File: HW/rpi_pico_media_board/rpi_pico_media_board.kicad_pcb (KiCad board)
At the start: 4 copper layers, 100 x 80 mm, 138 parts, among them J100 Barrel_Jack_Switch_Pin3Ring, J200 Conn_01x04_Pin, J201 Conn_01x04_Pin, J300 AudioJack3_Ground_SwitchTR, J301 Conn_01x03_Pin, J400 TF-01A, Q100 T2N7002AK, Q500 T2N7002AK, Q501 T2N7002AK, Q502 T2N7002AK, SW200 SW_DPDT_XLX, U100 HT7533-1, U101 HT7533-1, U200 RaspberryPi_Pico, U202 mems-mic, U203 mems-mic, U300 PCM5102A, U500 SW, U501 SW, U502 SW, U503 SW, U504 SW, U505 SW, U506 SW, U507 SW, U508 SW, U509 SW, U510 SW, U511 SW, U600 PCF8563TS, Y600 32768Hz

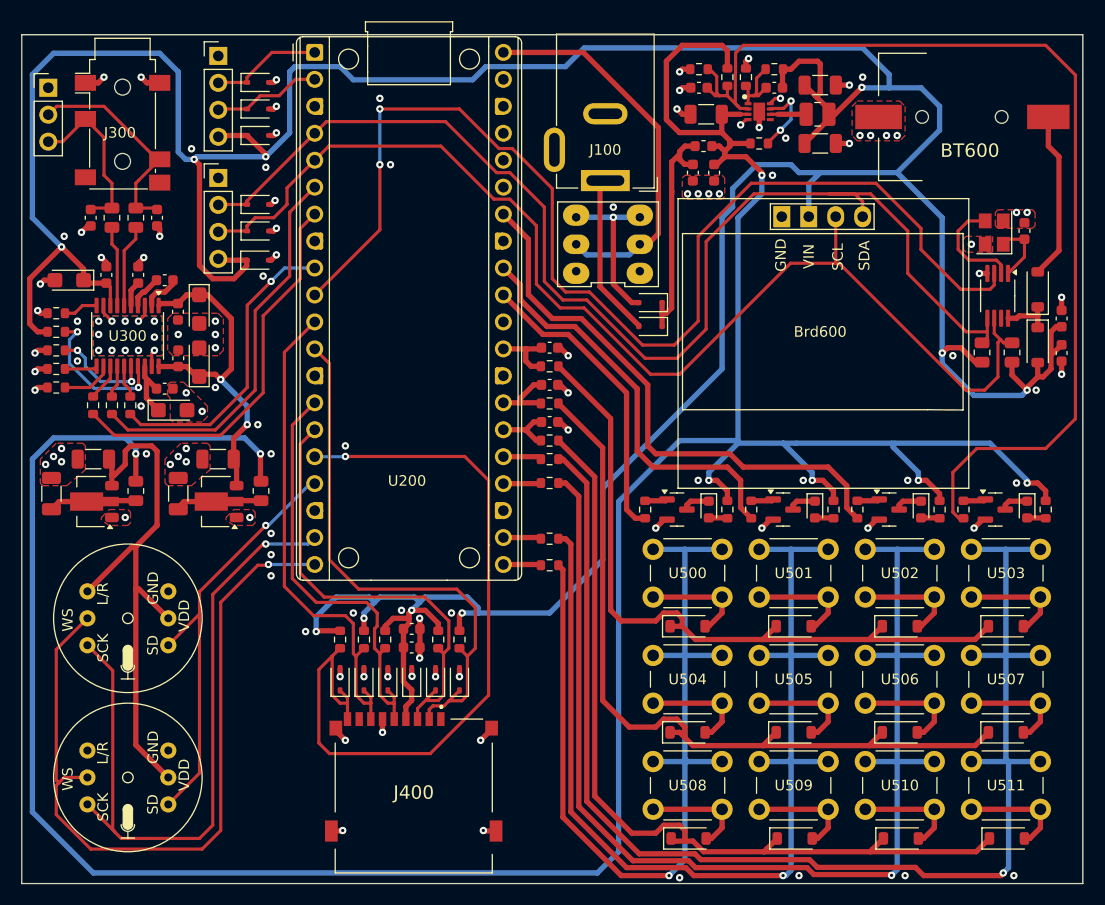
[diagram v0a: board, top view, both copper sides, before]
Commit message: Minor PCB layout updates
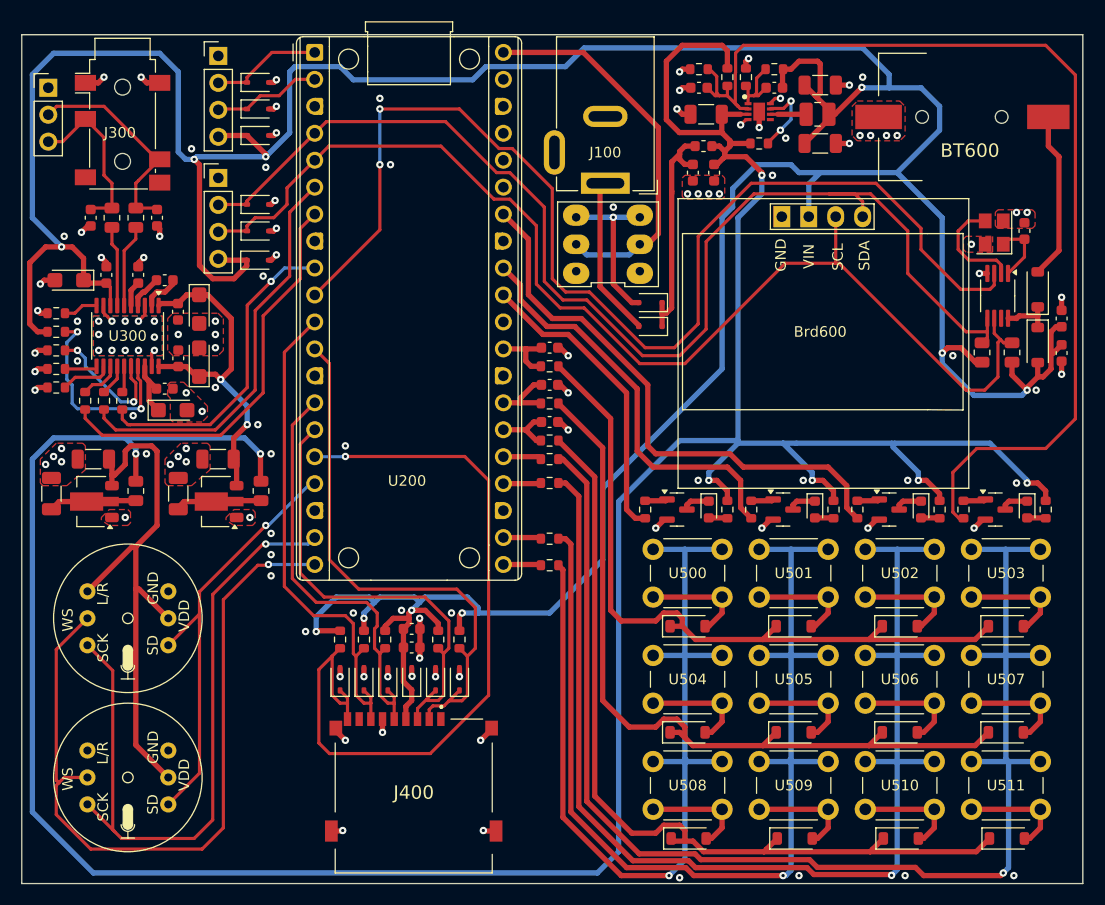
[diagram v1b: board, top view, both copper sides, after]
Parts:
- moved R300 0.86 mm to (59.5, 84.5)
- moved R301 0.86 mm to (57.8, 84.5)
- moved R302 0.86 mm to (56.0, 84.5)
- moved J100 0.25 mm to (105.0, 64.0)
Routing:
- net /[3]PCM5102/XSMT: track 14.7 -> 20.0 mm
- net /[3]PCM5102/FMT: track 10.4 -> 13.6 mm
- net I2S_PCM5102_SCL: track 28.5 -> 30.1 mm
- net +3.3V: track 368.0 -> 369.5 mm
- net I2S_PCM5102_DATA: track 37.1 -> 38.5 mm
- net I2S_PCM5102_SCK: track 37.4 -> 38.8 mm
- net I2C1_SCL: track 111.4 -> 110.6 mm
- net /[3]PCM5102/LRCLK: track 3.09 -> 2.50 mm

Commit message: Trace length tuning
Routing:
- net I2S_INMP441_DATA: track 41.4 -> 69.2 mm
- net SPI1_SD_CARD_SCK: track 40.2 -> 52.9 mm
- net SPI1_SD_CARD_MOSI: track 43.1 -> 54.4 mm
- net I2S_PCM5102_SCL: track 30.1 -> 38.5 mm
- net SPI1_SD_CARD_MISO: track 46.7 -> 53.7 mm
- net I2S_INMP441_SCK: track 65.6 -> 69.0 mm
- net SPI1_SD_CARD_CS: track 52.1 -> 55.5 mm
- net I2S_INMP441_SCL: track 72.2 -> 70.1 mm
- net +3.3V: track 369.5 -> 370.1 mm
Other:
- board text added: "3V3"
- board text added: "G"
- board text added: "INMP PWR"
- board text added: "L"
- board text added: "PCF8563TS"
- board text added: "PCM PWR"
- board text added: "PCM5102A"
- board text added: "Power Good"
- board text added: "R"
- board text added: "RX"
- board text added: "SCL"
- board text added: "SDA"
- board text added: "TX"
- board text added: "Use RPI VBUS"
